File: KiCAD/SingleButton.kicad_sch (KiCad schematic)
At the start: 2 parts

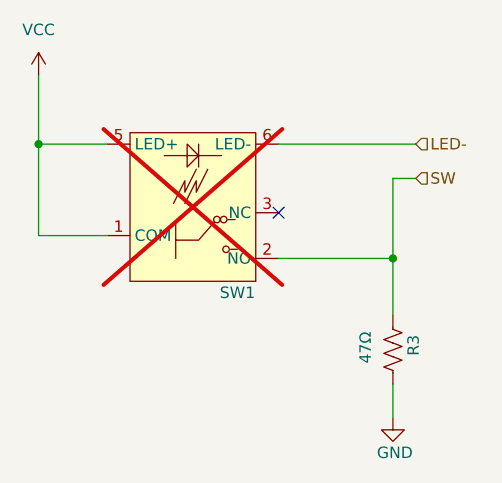
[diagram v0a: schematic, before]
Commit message: Revert "3 rows of 16 buttons; SMT"
This reverts commit c08e4dc0c350e57a2ca7329c2459be699e742724.
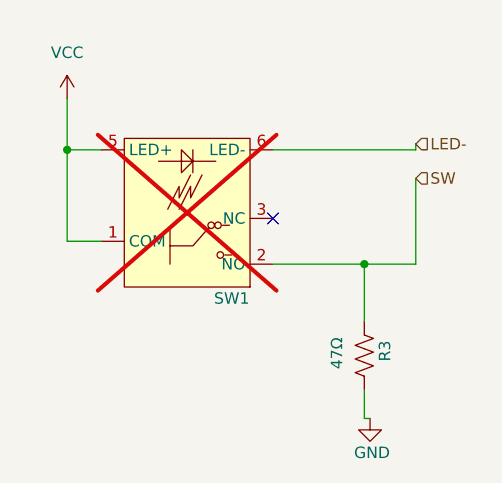
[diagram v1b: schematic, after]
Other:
- moved on the sheet: R3, SW1

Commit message: clean up SingleButton schematic
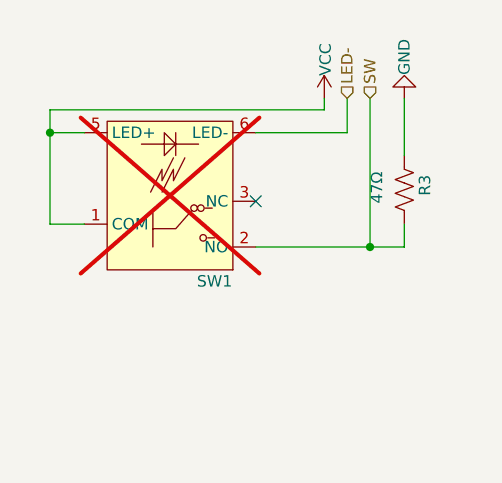
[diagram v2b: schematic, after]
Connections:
- net GND: now also R3.1; no longer R3.2
- net SW: now also R3.2; no longer R3.1
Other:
- moved on the sheet: R3, SW1
